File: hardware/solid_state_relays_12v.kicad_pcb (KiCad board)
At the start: 2 copper layers, 100 x 90 mm, 88 parts, among them J1 1190297, J2 1190297, J3 1190297, J4 1190297, J5 1190297, J6 1190297, J7 1190297, J8 1190297, M1 Fan, M2 Fan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

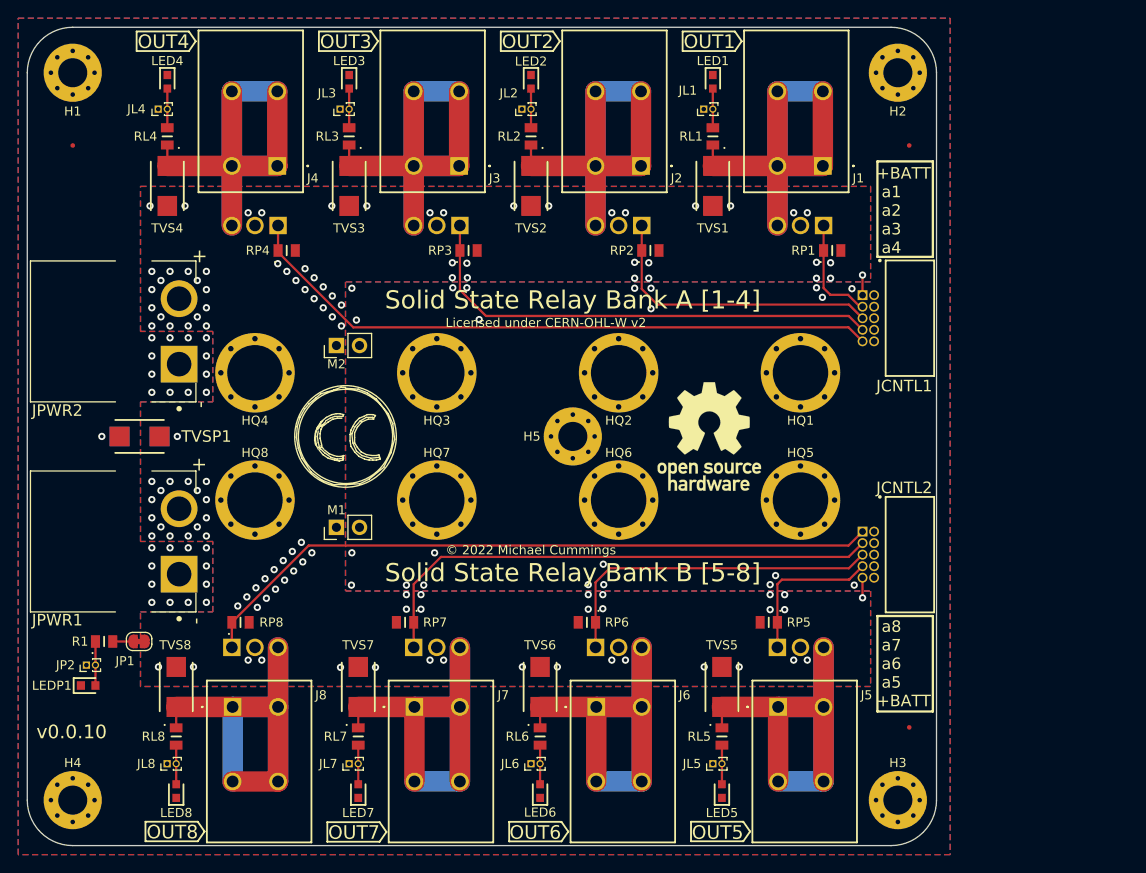
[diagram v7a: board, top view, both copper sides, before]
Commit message: Changed schematic to hierarchical style with mutliple sheets
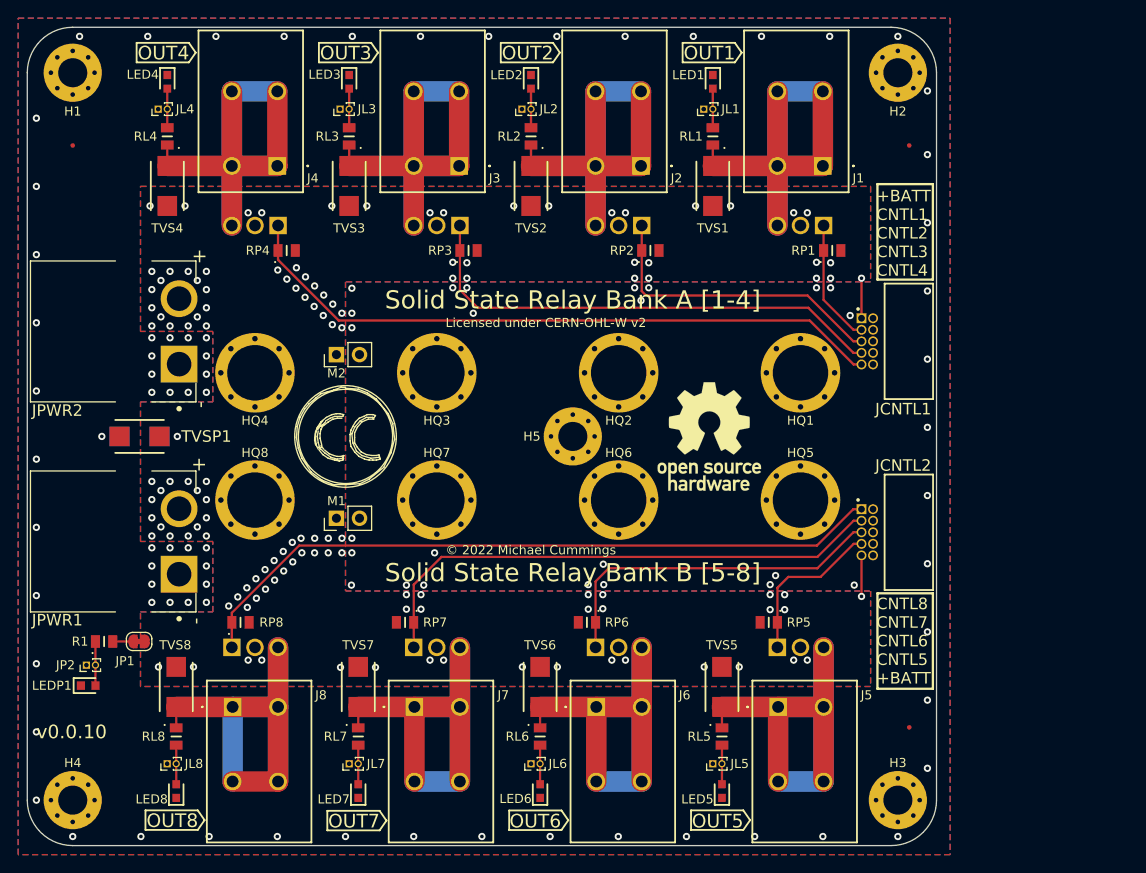
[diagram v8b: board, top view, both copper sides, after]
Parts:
- moved JCNTL1 2.54 mm to (107.4, 49.5)
- moved JCNTL2 2.46 mm to (107.4, 70.5)
- moved M1 1.00 mm to (49.0, 69.0)
- moved M2 1.00 mm to (49.0, 51.0)
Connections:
- net /a1 renamed /Control In - Power Out/BANK_A.CNTL1
- net /a2 renamed /Control In - Power Out/BANK_A.CNTL2
- net /a3 renamed /Control In - Power Out/BANK_A.CNTL3
- net /a4 renamed /Control In - Power Out/BANK_A.CNTL4
- net /a5 renamed /Control In - Power Out/BANK_B.CNTL5
- net /a6 renamed /Control In - Power Out/BANK_B.CNTL6
- net /a7 renamed /Control In - Power Out/BANK_B.CNTL7
- net /a8 renamed /Control In - Power Out/BANK_B.CNTL8
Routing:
- net +BATT: track 4.42 -> 8.92 mm, vias 119 -> 127
- net /Control In - Power Out/BANK_A.CNTL1: track 11.7 -> 13.7 mm
- net /Control In - Power Out/BANK_A.CNTL4: track 71.1 -> 72.7 mm
- net /Control In - Power Out/BANK_B.CNTL8: track 76.3 -> 77.8 mm
- net /Control In - Power Out/BANK_A.CNTL2: track 32.6 -> 33.7 mm
- net /Control In - Power Out/BANK_B.CNTL6: track 37.8 -> 38.7 mm
- net /Control In - Power Out/BANK_A.CNTL3: track 53.2 -> 54.1 mm
- net /Control In - Power Out/BANK_B.CNTL7: track 58.2 -> 59.1 mm
- net /Control In - Power Out/BANK_B.CNTL5: track 17.1 -> 17.8 mm
- net GNDPWR: vias 47 -> 97
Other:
- board text added: "+BATT CNTL1 CNTL2 CNTL3 CNTL4"
- board text added: "CNTL8 CNTL7 CNTL6 CNTL5 +BATT"
- board text removed: "+BATT a1 a2 a3 a4"
- board text removed: "a8 a7 a6 a5 +BATT"
